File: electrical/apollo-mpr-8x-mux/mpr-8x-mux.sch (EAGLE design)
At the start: 30 parts, among them IC1 LM1117-3V3, Q1 2N7002D, Q2 2N7002D, U2 MCP23017SS, X1 RJ45-8-2-CONEC-1, X2 RJ45-8-2-CONEC-1, X3 RJ45-8-2-CONEC-1, X4 RJ45-8-2-CONEC-1, X5 RJ45-8-2-CONEC-1, X6 RJ45-8-2-CONEC-1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

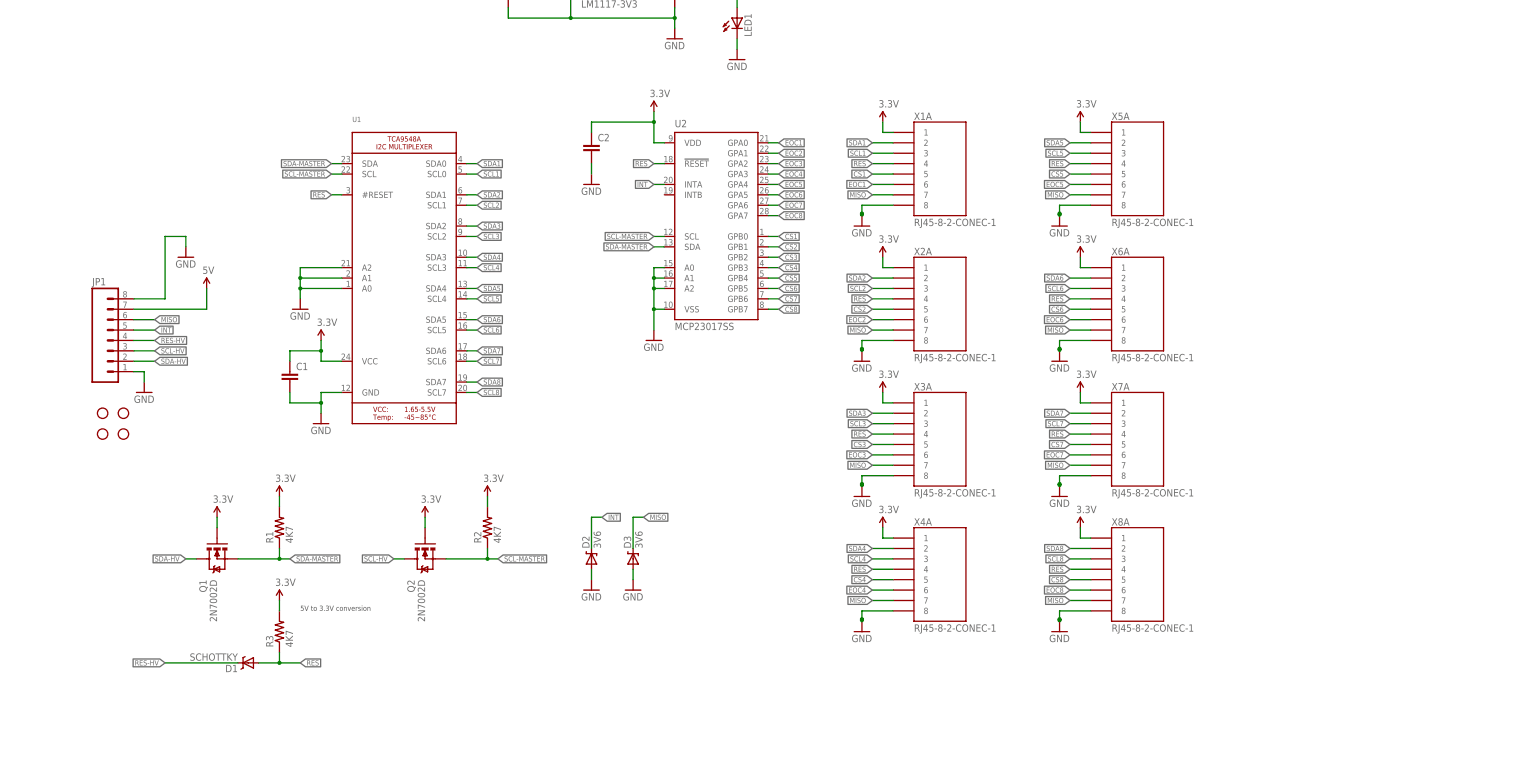
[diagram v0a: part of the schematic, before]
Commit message: fixed chip select problem with mosfets
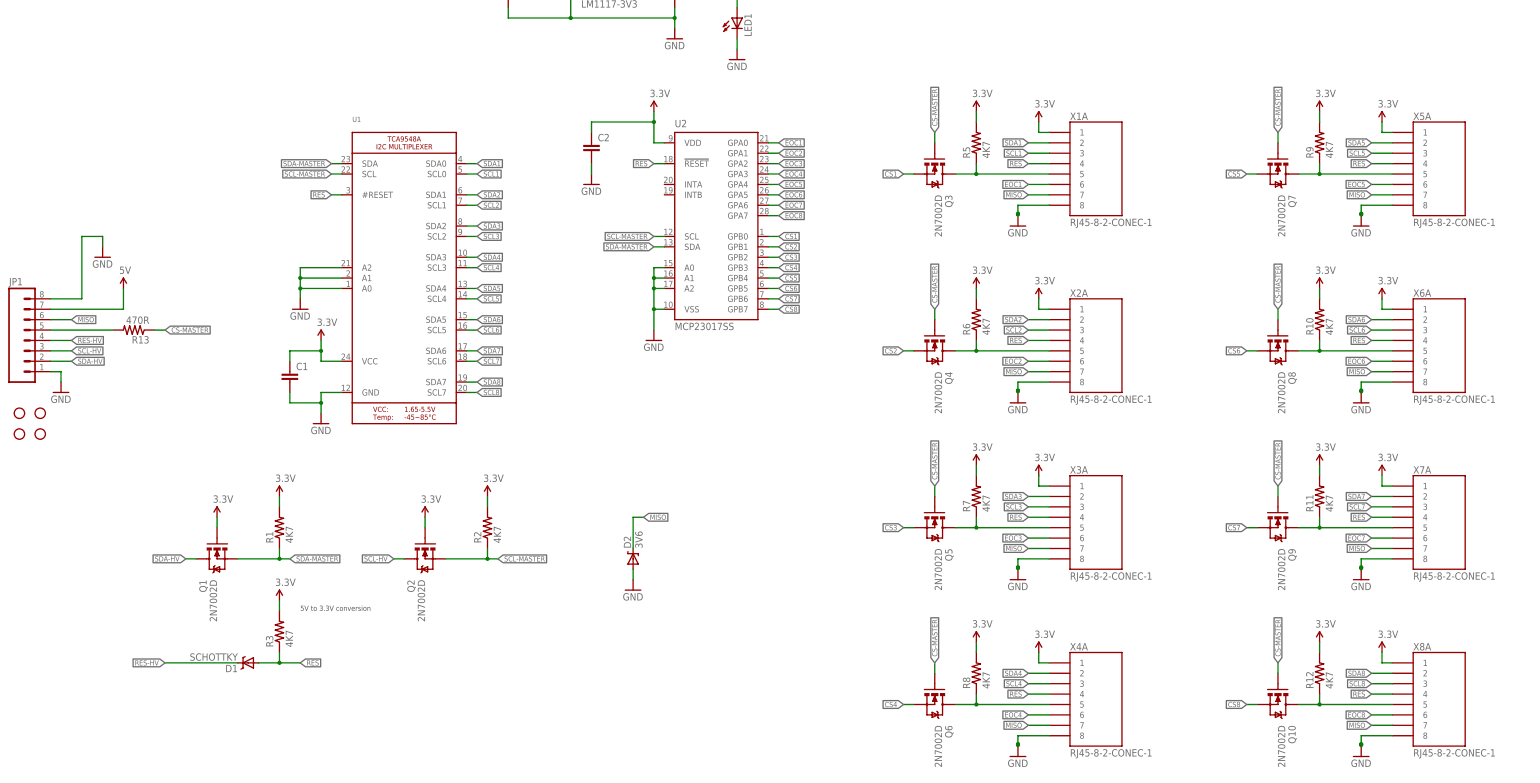
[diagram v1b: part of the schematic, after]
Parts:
- removed D3: 3V6, apollo-ctrl:DIODE-ZENERSOD
- added Q10, Q3, Q4, Q5, Q6, Q7, Q8, Q9: 2N7002D, apollo-ctrl:MOSFET-NCHANNELSMD
- added R10, R11, R12, R5, R6, R7, R8, R9: 4K7, apollo-ctrl:RESISTOR0805-RES
- added R13: 470R, apollo-ctrl:RESISTOR0805-RES
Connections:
- removed net INT: D2.C, JP1.5, U2.INTA
- new net CS-MASTER: Q10.G, Q3.G, Q4.G, Q5.G, Q6.G, Q7.G, Q8.G, Q9.G, R13.1
- new net N$10: JP1.5, R13.2
- new net N$2: Q7.D, R9.1, X5A.5
- new net N$3: Q8.D, R10.1, X6A.5
- new net N$4: Q9.D, R11.1, X7A.5
- new net N$5: Q10.D, R12.1, X8A.5
- new net N$6: Q6.D, R8.1, X4A.5
- new net N$7: Q5.D, R7.1, X3A.5
- new net N$8: Q4.D, R6.1, X2A.5
- new net N$9: Q3.D, R5.1, X1A.5
- net 3.3V: now also R10.2, R11.2, R12.2, R5.2, R6.2, R7.2, R8.2, R9.2
- net CS1: now also Q3.S; no longer X1A.5
- net CS2: now also Q4.S; no longer X2A.5
- net CS3: now also Q5.S; no longer X3A.5
- net CS4: now also Q6.S; no longer X4A.5
- net CS5: now also Q7.S; no longer X5A.5
- net CS6: now also Q8.S; no longer X6A.5
- net CS7: now also Q9.S; no longer X7A.5
- net CS8: now also Q10.S; no longer X8A.5
- net GND: no longer D3.A
- net MISO: now also D2.C; no longer D3.C
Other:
- moved on the sheet: D2, JP1, X1A, X2A, X3A, X4A, X5A, X6A, X7A, X8A

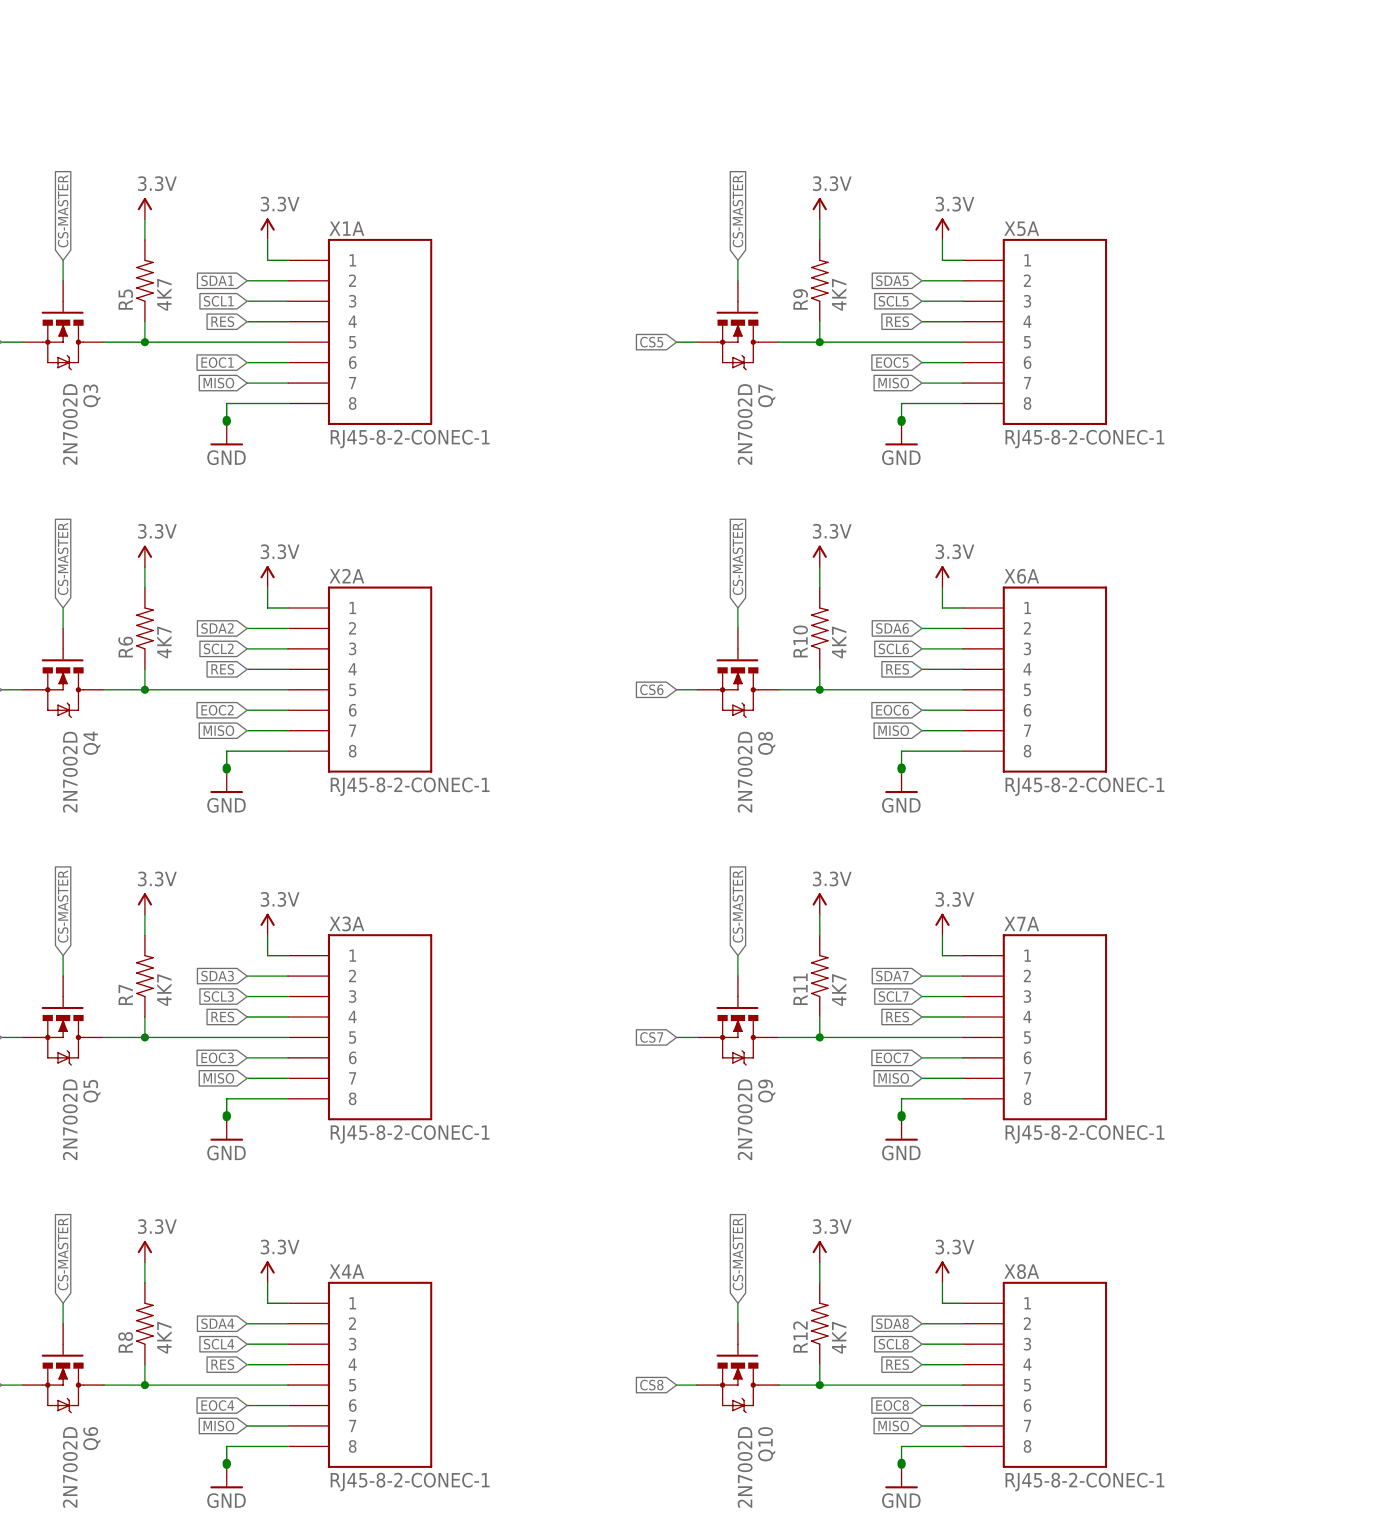
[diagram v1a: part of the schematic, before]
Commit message: added 2x4 header to mpr-8x-mux pcb
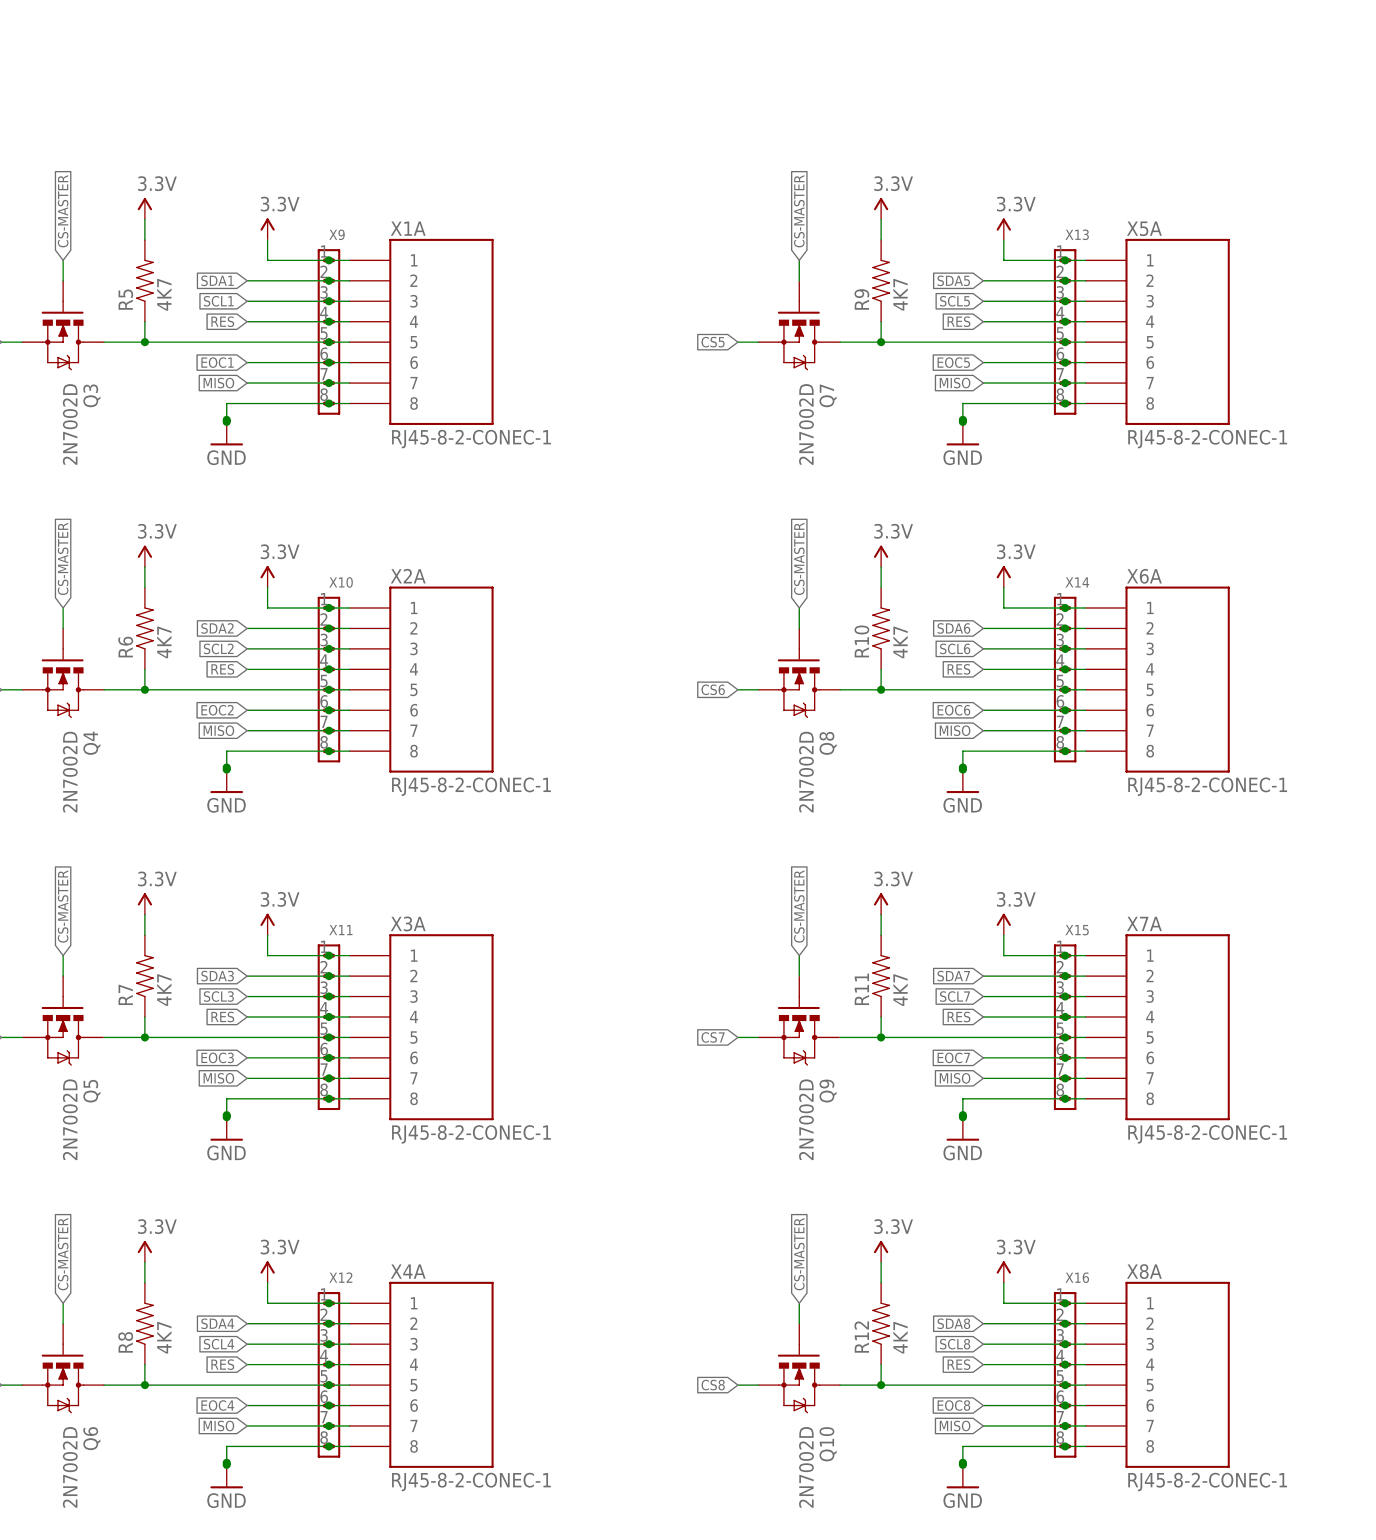
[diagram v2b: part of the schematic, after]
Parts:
- added X10, X11, X12, X13, X14, X15, X16, X9: TP-GROUP-X8-2X04, apollo-ctrl:TP-GROUP-X8-2X04
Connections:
- net 3.3V: now also X10.P$1, X11.P$1, X12.P$1, X13.P$1, X14.P$1, X15.P$1, X16.P$1, X9.P$1
- net EOC1: now also X9.P$6
- net EOC2: now also X10.P$6
- net EOC3: now also X11.P$6
- net EOC4: now also X12.P$6
- net EOC5: now also X13.P$6
- net EOC6: now also X14.P$6
- net EOC7: now also X15.P$6
- net EOC8: now also X16.P$6
- net GND: now also X10.P$8, X11.P$8, X12.P$8, X13.P$8, X14.P$8, X15.P$8, X16.P$8, X9.P$8
- net MISO: now also X10.P$7, X11.P$7, X12.P$7, X13.P$7, X14.P$7, X15.P$7, X16.P$7, X9.P$7
- net N$2: now also X13.P$5
- net N$3: now also X14.P$5
- net N$4: now also X15.P$5
- net N$5: now also X16.P$5
- net N$6: now also X12.P$5
- net N$7: now also X11.P$5
- net N$8: now also X10.P$5
- net N$9: now also X9.P$5
- net RES: now also X10.P$4, X11.P$4, X12.P$4, X13.P$4, X14.P$4, X15.P$4, X16.P$4, X9.P$4
- net SCL1: now also X9.P$3
- net SCL2: now also X10.P$3
- net SCL3: now also X11.P$3
- net SCL4: now also X12.P$3
- net SCL5: now also X13.P$3
- net SCL6: now also X14.P$3
- net SCL7: now also X15.P$3
- net SCL8: now also X16.P$3
- net SDA1: now also X9.P$2
- net SDA2: now also X10.P$2
- net SDA3: now also X11.P$2
- net SDA4: now also X12.P$2
- net SDA5: now also X13.P$2
- net SDA6: now also X14.P$2
- net SDA7: now also X15.P$2
- net SDA8: now also X16.P$2
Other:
- moved on the sheet: Q10, Q7, Q8, Q9, R10, R11, R12, R9, X1A, X2A, X3A, X4A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
